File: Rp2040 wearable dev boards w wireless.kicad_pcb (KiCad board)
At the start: 2 copper layers, 9.3 x 2.2 mm, 73 parts, among them IC1 NRF24L01P-R7, J1 battery plug, J2 UJ31-CH-31-SMT-TR, J3 Conn_01x22, J4 Conn_01x18, Q1 Si2301, SW1 B3U-1100P, U1 LTH7R, U2 W25Q128JVS, U3 TPD4E02B04QDQARQ1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

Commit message: finished schematic started pcb design, will need to review the power section.
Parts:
- added R18: 0, Resistor_SMD:R_0402_1005Metric, F.Cu at (83.5, 117.0)
- added TP1: 3.3v test point, TestPoint:TestPoint_Pad_D2.0mm, F.Cu at (77.0, 128.0)
- added TP2: ground test point, TestPoint:TestPoint_Pad_D2.0mm, F.Cu at (97.3, 111.5)
- added TP3: rf test point, TestPoint:TestPoint_Pad_D2.0mm, F.Cu at (255.8, 33.0)
- C11, C19: footprint Capacitor_SMD:C_01005_0402Metric -> Capacitor_SMD:CP_Elec_5x5.3
- C5, C9, D2, R2, R5, R8, R9, U3, U4: moved to B.Cu
- J3: value Conn_01x22 -> 3040-40-00; footprint Connector_PinSocket_2.54mm:PinSocket_1x22_P2.54mm_Horizontal -> Connector_IDC:IDC-Header_2x20_P2.54mm_Vertical
- J4: value Conn_01x18 -> serial wire debug port; footprint Connector_PinSocket_2.54mm:PinSocket_1x18_P2.54mm_Horizontal -> Connector_JST:JST_PH_S2B-PH-SM4-TB_1x02-1MP_P2.00mm_Horizontal
- U1: value LTH7R -> MCP73831T-4ADI/OT; moved to B.Cu
- moved U3 221.2 mm to (71.5, 117.0), turned to 90 degrees
- moved D1 217.7 mm to (77.0, 120.0), turned to 90 degrees
- moved R2 200.3 mm to (92.0, 114.5), turned to 90 degrees
- moved R9 191.2 mm to (73.0, 115.0), turned to 90 degrees
- moved J4 184.7 mm to (58.0, 125.0)
- moved R8 179.7 mm to (72.0, 115.0), turned to 90 degrees
- moved J2 175.4 mm to (70.0, 119.6)
- moved C1 174.6 mm to (93.7, 107.8)
- moved J1 166.7 mm to (94.0, 125.0), turned to 90 degrees
- moved Q1 161.4 mm to (83.5, 120.5)
- moved Y1 160.2 mm to (95.5, 101.1), turned to -90 degrees
- moved C9 154.5 mm to (81.0, 117.3), turned to -90 degrees
- moved R3 152.2 mm to (77.0, 124.0), turned to -90 degrees
- moved C8 151.4 mm to (68.7, 118.1), turned to 90 degrees
- moved C10 149.6 mm to (128.2, 57.0)
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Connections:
- C9 pad 1: +3.3V -> Net-(C9-Pad1)
- J4 pad 1: /VBUS -> /SWCLK
- J4 pad 2: +3.3V -> /SWD
- U4 pad 2: +3.3V -> Net-(C9-Pad1)
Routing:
- net /VBUS: track 0.00 -> 21.6 mm, vias 0 -> 3
- net GND: track 0.00 -> 20.2 mm, vias 0 -> 8
- net Net-(C5-Pad1): track 0.00 -> 19.7 mm, vias 0 -> 2
- net Net-(C9-Pad1): track 0.00 -> 19.0 mm, vias 0 -> 2
- net Net-(R3-Pad2): track 0.00 -> 17.4 mm, vias 0 -> 1
- net Net-(J2-PadB5): track 0.00 -> 15.0 mm, vias 0 -> 1
- net /VBAT: track 0.00 -> 11.2 mm, vias 0 -> 1
- net Net-(J2-PadA5): track 0.00 -> 8.87 mm, vias 0 -> 1
- net /USB+: track 0.00 -> 6.87 mm, vias 0 -> 1
- net /USB-: track 0.00 -> 4.94 mm, vias 0 -> 1
- net Net-(D1-Pad1): track 0.00 -> 2.70 mm
- net Net-(R2-Pad1): track 0.00 -> 1.87 mm
- net +3.3V: track 0.00 -> 1.71 mm, vias 0 -> 1
- added copper zone on In2.Cu, net +3.3V
- added copper zone on In2.Cu, net /VBUS
- added copper zone on In1.Cu, net GND
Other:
- board size 9.3 x 2.2 mm -> 44.9 x 70.6 mm
- copper layers 2 -> 4

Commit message: mmmmmmmmmmm change log.exe
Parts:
- removed AE1: Antenna, coaxial conn:MURATA_MM8030-2610RJ3
- added J5: Conn_01x04, Connector_PinSocket_2.54mm:PinSocket_2x02_P2.54mm_Horizontal, F.Cu at (38.7, 86.4)
- added J6: EMPCB.SMAFSTJ.B.HT, EMPCB.SMAFSTJ.B:TAOGLAS_EMPCB.SMAFSTJ.B.HT, F.Cu at (73.5, 37.8)
- added SW2: power Switch, Connector_JST:JST_PH_S2B-PH-SM4-TB_1x02-1MP_P2.00mm_Horizontal, F.Cu at (71.0, 74.0)
- C5, C9, D2, R2, R5, R8, R9, U1: moved to F.Cu
- J3: value 3040-40-00 -> Conn_01x20; footprint Connector_IDC:IDC-Header_2x20_P2.54mm_Vertical -> Connector_FFC-FPC:TE_2-84952-0_1x20-1MP_P1.0mm_Horizontal
- J4: value serial wire debug port -> Conn_01x20; footprint Connector_JST:JST_PH_S2B-PH-SM4-TB_1x02-1MP_P2.00mm_Horizontal -> Connector_FFC-FPC:TE_2-84952-0_1x20-1MP_P1.0mm_Horizontal
- U3: footprint TPD4E02B04QDQARQ1:TPD4E02B04QDQARQ1 -> LIB_TPD4E02B04QDQARQ1:TPD4E02B04QDQARQ1; moved to F.Cu
- U4: footprint Package_TO_SOT_SMD:TO-252-2 -> Package_TO_SOT_SMD:SOT-223; moved to F.Cu
- moved U7 236.5 mm to (49.5, 38.0)
- moved U6 214.2 mm to (59.0, 38.0), turned to -90 degrees
- moved C23 192.2 mm to (94.5, 66.5)
- moved C21 189.9 mm to (93.3, 68.5)
- moved IC1 185.1 mm to (72.0, 48.0), turned to 90 degrees
- moved C12 183.2 mm to (88.9, 73.3)
- moved C22 182.3 mm to (97.8, 82.9)
- moved Y2 182.2 mm to (73.0, 53.5), turned to 180 degrees
- moved C11 176.2 mm to (100.8, 49.6)
- moved R13 171.2 mm to (89.3, 71.5)
- moved R10 168.5 mm to (105.2, 66.6)
- moved C24 165.4 mm to (95.5, 82.1)
- moved C25 165.0 mm to (95.5, 83.7)
- moved C26 158.5 mm to (97.4, 64.3)
- moved R14 157.6 mm to (104.0, 74.6)
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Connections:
- net +1V1 renamed /DVDD_RP2040
- net /refin renamed /REFin/REFout
- net Net-(AE1-Pad1) renamed /Antenna
- net Net-(C11-Pad1) renamed /ADC VDD
- net Net-(C23-Pad1) renamed /REGOUT
- net Net-(C28-Pad1) renamed /DVDD_RADIO
- net Net-(C31-Pad1) renamed /L2-C31
- net Net-(C5-Pad1) renamed /VI
- net Net-(C9-Pad1) renamed /VO
- net Net-(D1-Pad1) renamed /LED_BLUE
- net Net-(D4-Pad2) renamed /LED_GREEN
- net Net-(IC1-Pad16) renamed /IREF
- net Net-(R2-Pad1) renamed /PROG
- net Net-(R3-Pad2) renamed /STAT
- net Net-(R6-Pad2) renamed /USB_R+
- net Net-(R7-Pad2) renamed /USB_R-
- net Net-(SW1-Pad1) renamed /SW1 
- C10 pad 1: +3.3V -> /Vmain
- C13 pad 1: +3.3V -> /Vmain
- C14 pad 1: +3.3V -> /Vmain
- C15 pad 1: +3.3V -> /Vmain
- C16 pad 1: +3.3V -> /Vmain
- C17 pad 1: +3.3V -> /Vmain
- C18 pad 1: +3.3V -> /Vmain
- C19 pad 1: +3.3V -> /Vmain
- C20 pad 1: +3.3V -> /Vmain
- C21 pad 1: +3.3V -> /Vmain
- C22 pad 1: +3.3V -> /Vmain
- C26 pad 1: +3.3V -> /Vmain
- C27 pad 1: +3.3V -> /Vmain
- C3 pad 1: +3.3V -> /Vmain
- IC1 pad 15: +3.3V -> /Vmain
- IC1 pad 18: +3.3V -> /Vmain
- IC1 pad 7: +3.3V -> /Vmain
- J2 pad A5: Net-(J2-PadA5) -> /CC1
- J2 pad A6: /USB+ -> /USB-
- J2 pad A7: /USB- -> /USB+
- J2 pad B5: Net-(J2-PadB5) -> /CC2
- J2 pad B6: /USB+ -> /USB-
- J2 pad B7: /USB- -> /USB+
- J3 pad 16: /GPIO 16 -> /RUN
- J3 pad 17: /GPIO 17 -> /SWCLK
- J3 pad 18: /IMU SDA / GPIO 18 -> /SWD
- J3 pad 19: /IMU SCL / GPIO 19 -> /Vmain
- J3 pad 20: /External ADC SDA / GPIO 20 -> GND
- J4 pad 1: /SWCLK -> /GPIO 0
- J4 pad 2: /SWD -> /GPIO 16
- R10 pad 2: +3.3V -> /Vmain
- R11 pad 1: +3.3V -> /Vmain
- R12 pad 1: +3.3V -> /Vmain
- R16 pad 1: +3.3V -> /Vmain
- R17 pad 1: +3.3V -> /Vmain
- R18 pad 2: +3.3V -> /R18-Power_on
- R8 pad 1: Net-(J2-PadB5) -> /CC1
- R9 pad 1: Net-(J2-PadA5) -> /CC2
- U2 pad 8: +3.3V -> /Vmain
- U3 pad 1: Net-(J2-PadA5) -> /CC2
- U3 pad 10: Net-(J2-PadA5) -> /CC2
- U3 pad 2: Net-(J2-PadB5) -> /CC1
- U3 pad 9: Net-(J2-PadB5) -> /CC1
- U5 pad 1: +3.3V -> /Vmain
- U5 pad 10: +3.3V -> /Vmain
- U5 pad 22: +3.3V -> /Vmain
- U5 pad 33: +3.3V -> /Vmain
- U5 pad 42: +3.3V -> /Vmain
- U5 pad 43: +3.3V -> /Vmain
- U5 pad 44: +3.3V -> /Vmain
- U5 pad 48: +3.3V -> /Vmain
- U5 pad 49: +3.3V -> /Vmain
- U7 pad 13: +3.3V -> /Vmain
- U7 pad 8: +3.3V -> /Vmain
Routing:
- net /CC2: track 0.00 -> 21.3 mm
- net /VI: track 19.7 -> 0.00 mm, vias 2 -> 0
- net /VO: track 19.0 -> 0.00 mm, vias 2 -> 0
- net /VBUS: track 21.6 -> 2.66 mm, vias 3 -> 0
- net /STAT: track 17.4 -> 0.00 mm, vias 1 -> 0
- net GND: track 20.2 -> 3.56 mm, vias 8 -> 1
- net Net-(J2-PadB5): track 15.0 -> 0.00 mm, vias 1 -> 0
- net /VBAT: track 11.2 -> 0.00 mm, vias 1 -> 0
- net Net-(J2-PadA5): track 8.87 -> 0.00 mm, vias 1 -> 0
- net /CC1: track 0.00 -> 7.31 mm
- net /LED_BLUE: track 2.70 -> 0.00 mm
- net /USB-: track 4.94 -> 7.42 mm
- net /PROG: track 1.87 -> 0.00 mm
- net +3.3V: track 1.71 -> 0.00 mm, vias 1 -> 0
- net /USB+: track 6.87 -> 5.60 mm, vias 1 -> 0
- removed copper zone on In2.Cu, net +3.3V
- removed copper zone on In2.Cu, net /VBUS
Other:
- board size 44.9 x 70.6 mm -> 40 x 75 mm

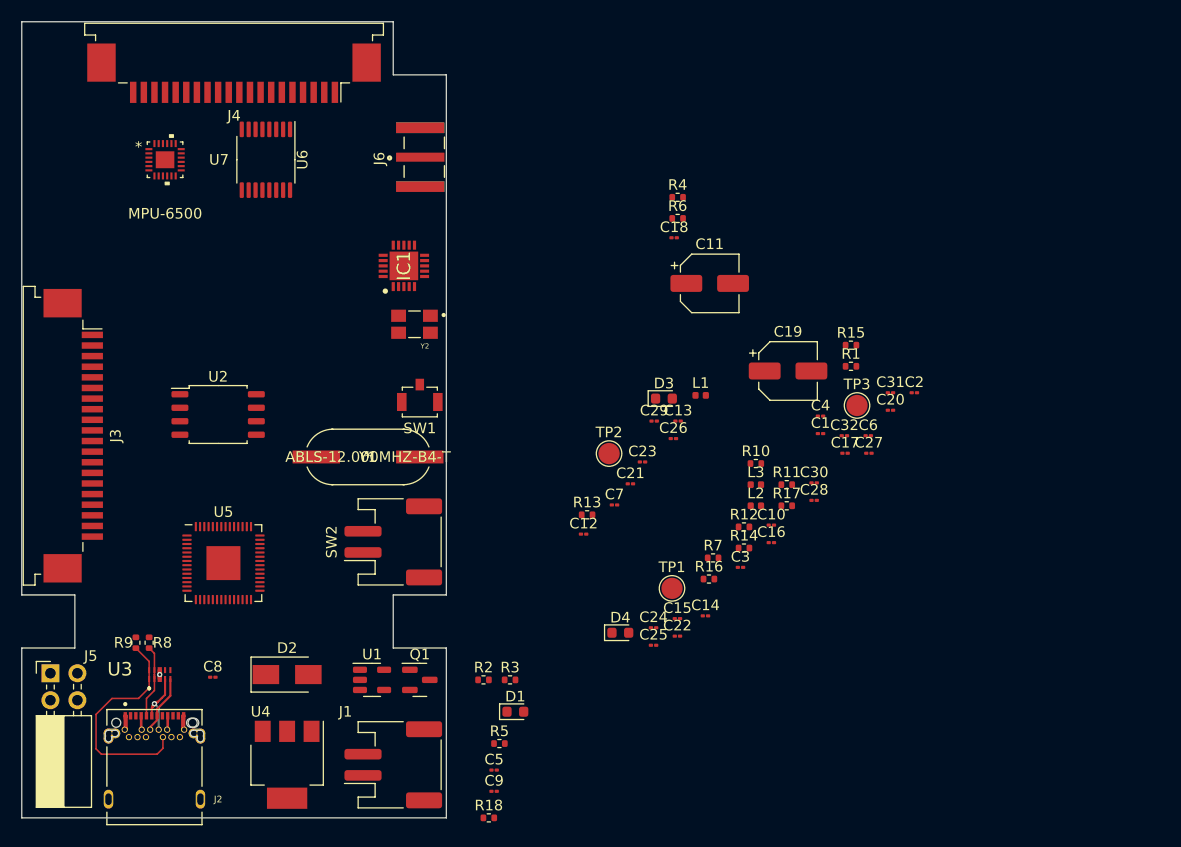
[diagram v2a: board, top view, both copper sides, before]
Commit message: routed power
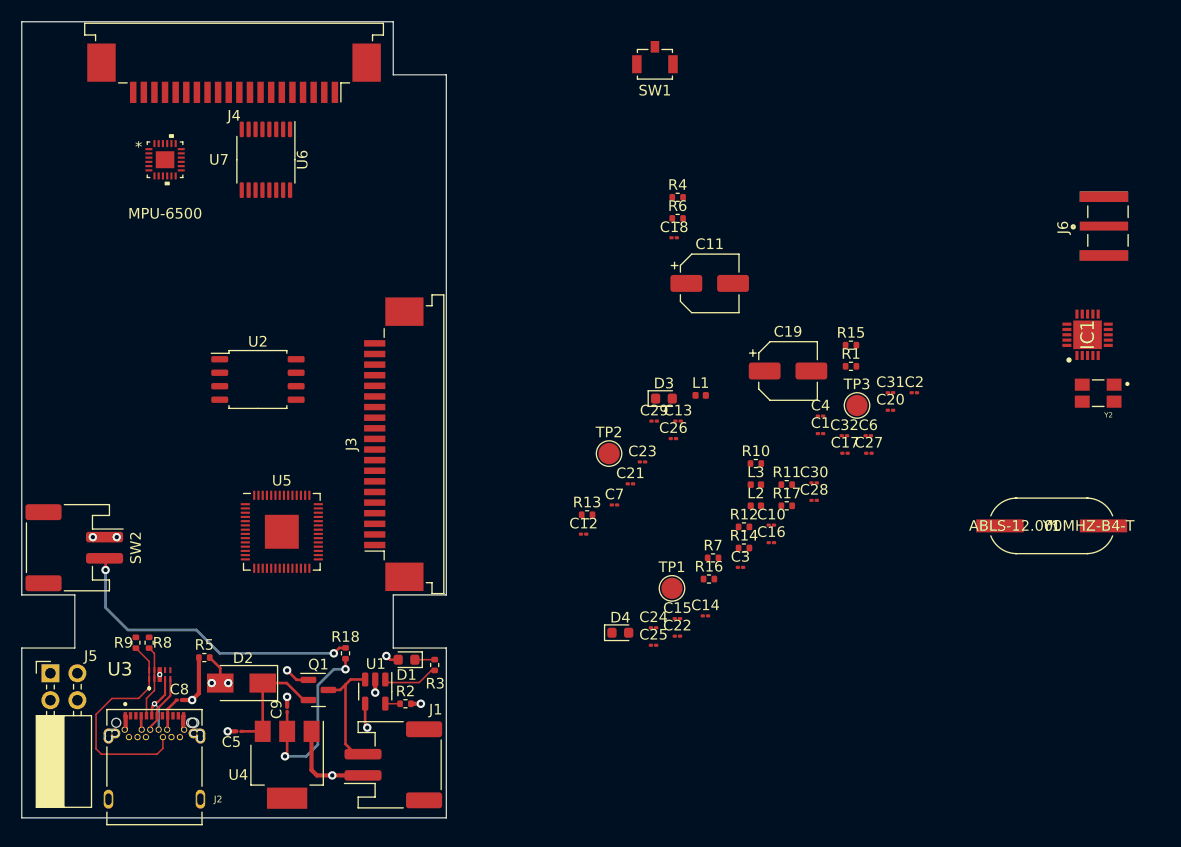
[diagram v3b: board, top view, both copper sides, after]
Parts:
- moved IC1 64.7 mm to (136.4, 54.5)
- moved Y2 64.7 mm to (137.4, 60.0)
- moved J6 64.7 mm to (137.9, 44.2)
- moved Y1 64.7 mm to (133.0, 72.5)
- moved SW1 38.8 mm to (95.7, 28.2)
- moved J3 30.2 mm to (71.0, 64.8), turned to 90 degrees
- moved SW2 30.1 mm to (41.0, 74.5), turned to -90 degrees
- moved R5 29.0 mm to (53.2, 84.9), turned to 180 degrees
- moved C5 24.3 mm to (56.5, 91.8), turned to 180 degrees
- moved C9 21.0 mm to (61.0, 89.8), turned to 90 degrees
- moved R18 20.6 mm to (66.5, 84.5), turned to 90 degrees
- moved D1 11.4 mm to (72.2, 85.1), turned to 180 degrees
- moved Q1 9.60 mm to (64.0, 88.0)
- moved R2 7.69 mm to (72.2, 89.2)
- moved R3 7.24 mm to (74.9, 85.6), turned to -90 degrees
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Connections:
- SW2 pad 1: /R18-Power_on -> /Vmain
- SW2 pad 2: /Vmain -> /R18-Power_on
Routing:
- net /R18-Power_on: track 0.00 -> 29.3 mm, vias 0 -> 2
- net GND: track 3.56 -> 21.4 mm, vias 1 -> 7
- net /VO: track 0.00 -> 17.6 mm, vias 0 -> 2
- net /VBAT: track 0.00 -> 12.0 mm
- net /VI: track 0.00 -> 11.1 mm
- net /VBUS: track 2.66 -> 12.8 mm, vias 0 -> 5
- net /STAT: track 0.00 -> 5.24 mm
- net /LED_BLUE: track 0.00 -> 1.87 mm
- net /PROG: track 0.00 -> 1.40 mm
- net /Vmain: vias 0 -> 2
- added copper zone on In2.Cu, net /VBUS

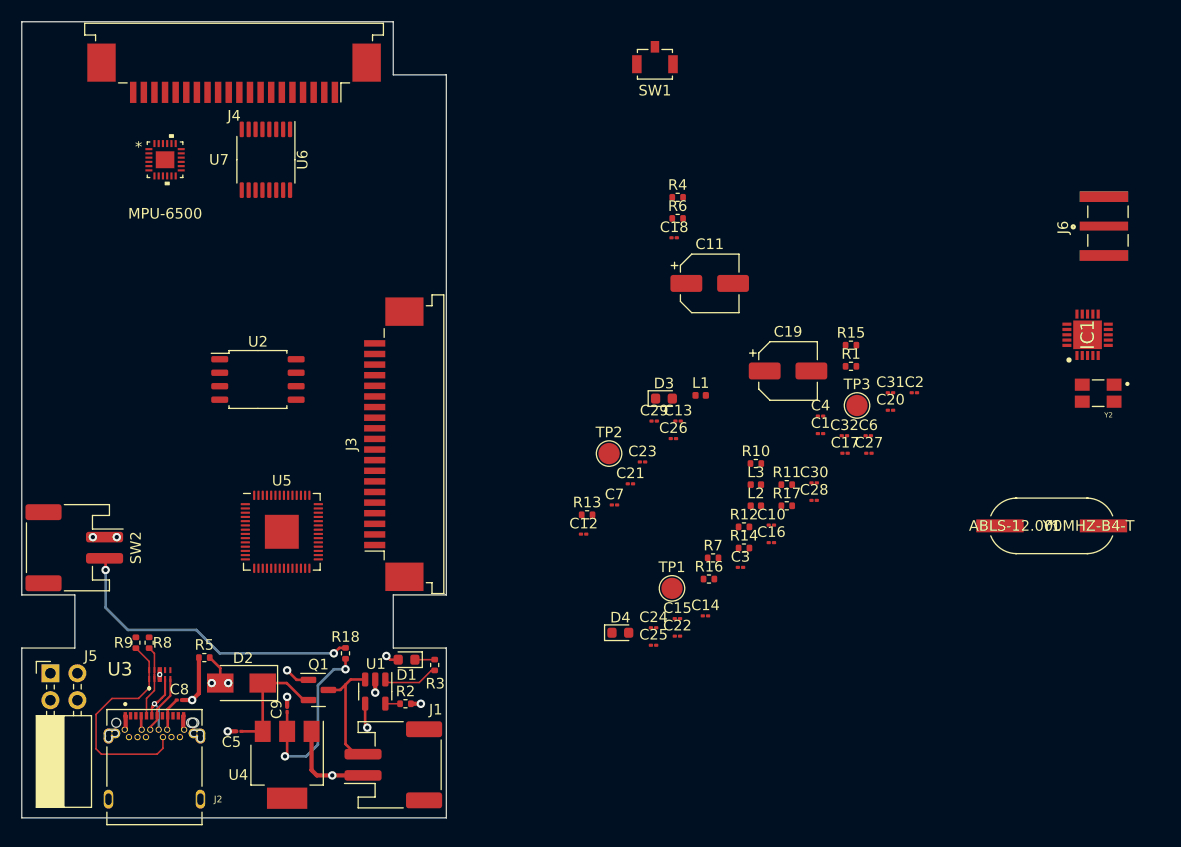
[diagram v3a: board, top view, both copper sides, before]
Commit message: started pinning out Rp2040 shortened board to 60 something long
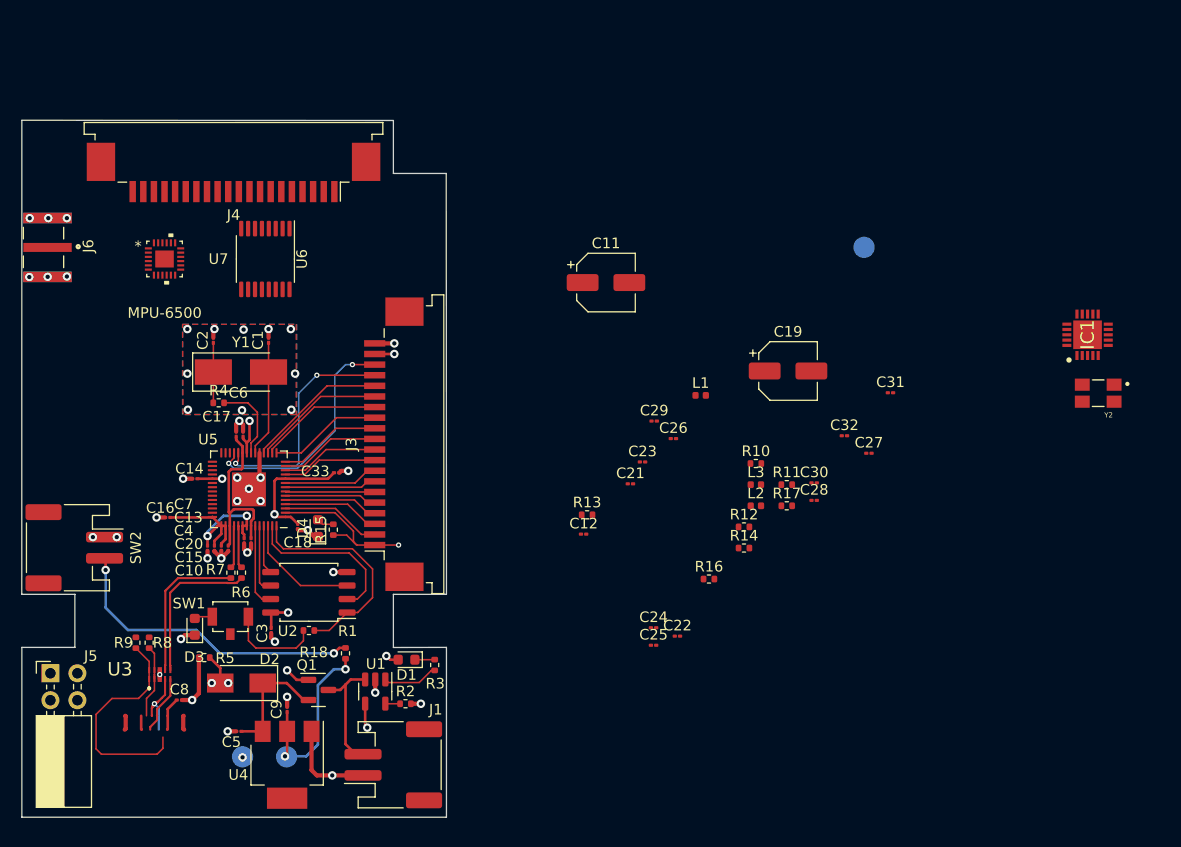
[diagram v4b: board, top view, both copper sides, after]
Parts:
- removed J2: UJ31-CH-31-SMT-TR, usb-c footprint:CUI_UJ31-CH-31-SMT-TR
- added C33: 100n, Capacitor_SMD:C_01005_0402Metric, F.Cu at (65.7, 67.5)
- TP1, TP2, TP3: moved to B.Cu
- Y1: value ABLS-12.000MHZ-B4-T -> 445C25D12M00000; footprint ABLS-12:ABLS-12.000MHZ-B4-T -> Crystal:Crystal_SMD_5032-2Pin_5.0x3.2mm_HandSoldering
- moved J6 99.5 mm to (38.4, 46.3), turned to -90 degrees
- moved Y1 77.7 mm to (56.6, 58.0)
- moved SW1 67.0 mm to (55.6, 81.9), turned to 0 degrees
- moved C2 66.2 mm to (54.0, 55.0), turned to 90 degrees
- moved C20 64.4 mm to (54.8, 74.6), turned to -90 degrees
- moved C6 59.6 mm to (56.2, 63.9), turned to 90 degrees
- moved C4 57.2 mm to (55.5, 74.6), turned to -90 degrees
- moved C16 56.9 mm to (49.8, 71.7), turned to 180 degrees
- moved R1 56.8 mm to (63.0, 82.3)
- moved C17 56.7 mm to (56.9, 63.9), turned to 90 degrees
- moved C10 53.2 mm to (53.5, 74.6), turned to -90 degrees
- moved R6 52.9 mm to (56.7, 76.9), turned to 90 degrees
- moved C1 52.7 mm to (59.2, 55.0), turned to 90 degrees
- moved R15 51.8 mm to (65.3, 72.8), turned to 90 degrees
- moved C14 49.8 mm to (52.3, 68.0), turned to 180 degrees
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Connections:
- J3 pad 10: /GPIO 10 -> /GPIO 9
- J3 pad 11: /GPIO 11 -> /GPIO 10
- J3 pad 12: /GPIO 12 -> /GPIO 11
- J3 pad 13: /GPIO 13 -> /GPIO 12
- J3 pad 14: /GPIO 14 -> /GPIO 13
- J3 pad 15: /GPIO 15 -> /GPIO 14
- J3 pad 16: /RUN -> /GPIO 15
- J3 pad 3: /GPIO 3 -> /GPIO 2
- J3 pad 4: /GPIO 4 -> /GPIO 3
- J3 pad 5: /GPIO 5 -> /GPIO 4
- J3 pad 6: /GPIO 6 -> /GPIO 5
- J3 pad 7: /GPIO 7 -> /GPIO 6
- J3 pad 8: /GPIO 8 -> /GPIO 7
- J3 pad 9: /GPIO 9 -> /GPIO 8
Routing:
- net /Vmain: track 0.00 -> 44.7 mm, vias 2 -> 9
- net /SWD: track 0.00 -> 22.3 mm, vias 0 -> 2
- net /SWCLK: track 0.00 -> 22.1 mm, vias 0 -> 2
- net GND: track 21.4 -> 43.3 mm, vias 7 -> 41
- net /QSPI_SS: track 0.00 -> 21.1 mm
- net /DVDD_RP2040: track 0.00 -> 16.9 mm
- net /QSPI_SD1: track 0.00 -> 15.6 mm
- net /GPIO 0: track 0.00 -> 15.1 mm, vias 0 -> 1
- net /USB+: track 5.60 -> 20.2 mm
- net /USB-: track 7.42 -> 21.6 mm
- net /GPIO 15: track 0.00 -> 13.3 mm
- net /GPIO 14: track 0.00 -> 12.5 mm
- net /GPIO 13: track 0.00 -> 11.6 mm
- net /QSPI_SD2: track 0.00 -> 11.3 mm
- net /XIN: track 0.00 -> 10.9 mm
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- added copper zone on B.Cu, net (none)
- added copper zone on In2.Cu, net /Vmain
- added copper zone on F.Cu, net GND
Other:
- board size 40 x 75 mm -> 40 x 65.7 mm
